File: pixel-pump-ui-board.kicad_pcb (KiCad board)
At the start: 4 copper layers, 36.4 x 48.3 mm, 49 parts, among them J1 BM10B-SRSS-TB(LF)(SN), SW1 LIFT, SW2 LOW, SW3 REVERSE, SW4 TRIGGER, SW5 DROP, SW6 HIGH, U1 WS2812-2020, U10 WS2812-2020, U11 WS2812-2020, U12 WS2812-2020, U2 WS2812-2020, U3 WS2812-2020, U4 WS2812-2020, U5 WS2812-2020, U6 WS2812-2020, U7 WS2812-2020, U8 WS2812-2020, U9 WS2812-2020

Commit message: Updated ref label on board
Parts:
- removed kibuzzard-61084764: G***, kibuzzard-61084764
- added kibuzzard-61E47AFB: G***, kibuzzard-61E47AFB, B.Cu at (82.0, 97.6)

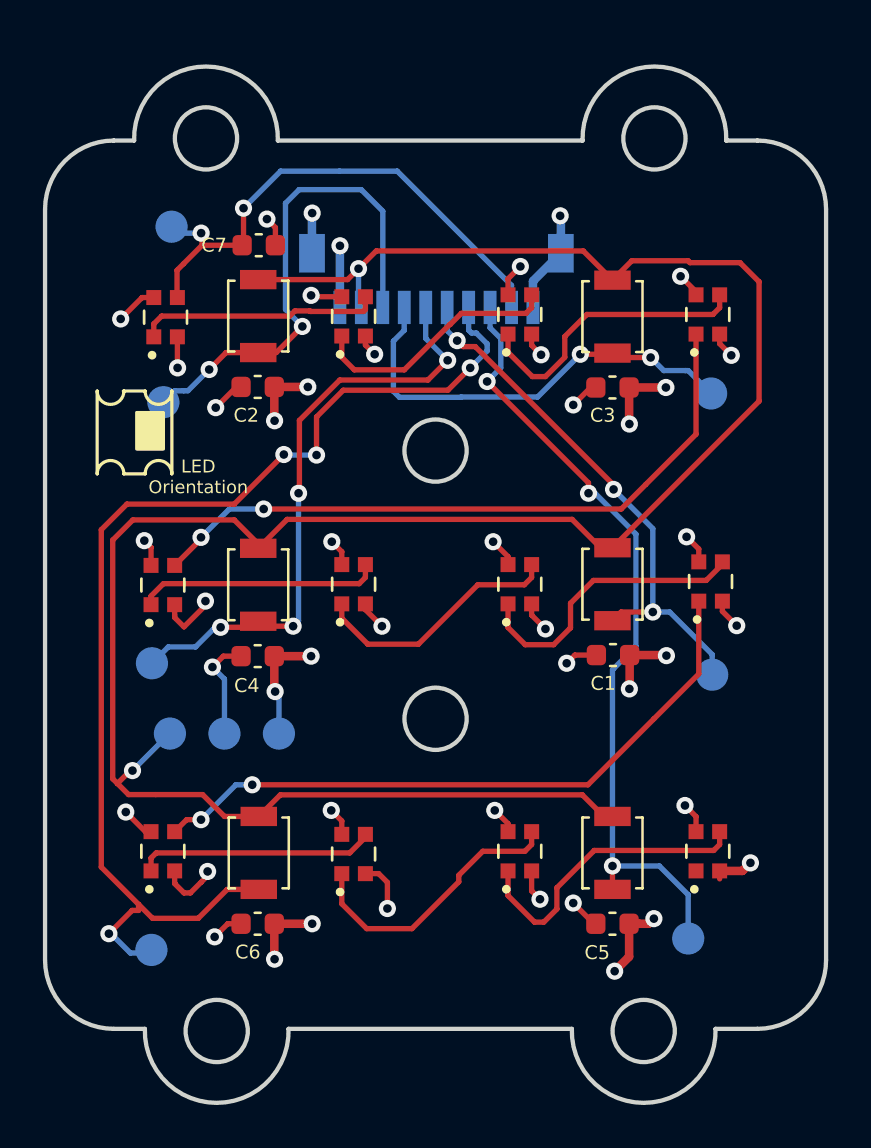
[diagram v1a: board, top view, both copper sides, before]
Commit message: Add side load connector to PCB & MPN to all parts
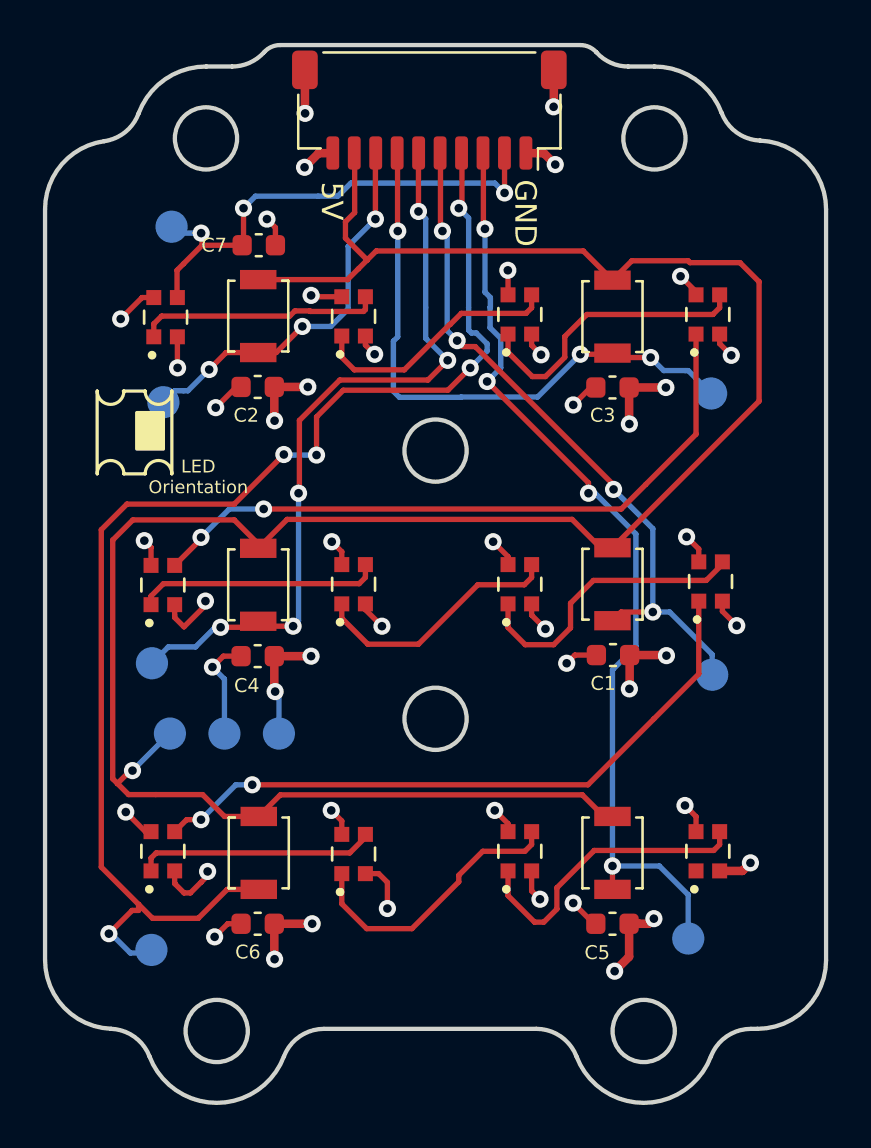
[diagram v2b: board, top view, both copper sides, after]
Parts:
- removed kibuzzard-61E47AFB: G***, kibuzzard-61E47AFB
- J1: value BM10B-SRSS-TB(LF)(SN) -> SM10B-SRSS-TB; footprint BM10B-SRSS-TB(LF)(SN):BM10B-SRSS-TB(LF)(SN) -> Connector_JST:JST_SH_SM10B-SRSS-TB_1x10-1MP_P1.00mm_Horizontal; moved to F.Cu
- SW1: value LIFT -> B3U-1000P
- SW2: value LOW -> B3U-1000P
- SW3: value REVERSE -> B3U-1000P
- SW4: value TRIGGER -> B3U-1000P
- SW5: value DROP -> B3U-1000P
- SW6: value HIGH -> B3U-1000P
- U1, U10, U11, U12, U2, U3, U4, U5, U6, U7, U8, U9: value WS2812-2020 -> WS2812B-2020
- moved J1 9.20 mm to (81.6, 64.5)
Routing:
- net LOW_BTN: track 28.2 -> 35.5 mm, vias 4 -> 5
- net TRIGGER_BTN: track 37.2 -> 44.5 mm, vias 3 -> 4
- net HIGH_BTN: track 25.1 -> 32.4 mm, vias 3 -> 4
- net REVERSE_BTN: track 54.4 -> 61.6 mm, vias 4 -> 5
- net DROP_BTN: track 20.7 -> 27.7 mm, vias 2 -> 3
- net LIFT_BTN: track 23.7 -> 18.2 mm, vias 2 -> 3
- net +3V3: track 107.6 -> 110.9 mm, vias 2 -> 1
- net +5V: track 32.4 -> 30.5 mm
- net GND: track 51.1 -> 49.4 mm, vias 27 -> 28
- net LED_DATA: track 25.1 -> 23.3 mm, vias 2 -> 3
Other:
- board size 36.4 x 48.3 mm -> 36.4 x 49.3 mm
- board text added: "REV 4"
- board text removed: "by Robin Reiter Hergatz, DE Aug 2021"
